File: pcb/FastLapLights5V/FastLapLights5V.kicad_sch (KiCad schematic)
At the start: 25 parts, among them IC1 74HCT1G125GV,125, J1 POWER_CON, J2 SWD, J3 I2C, J4 IO, U1 STM32C011F4Px, U2 AP63205WU, U3 AP2112K-3.3

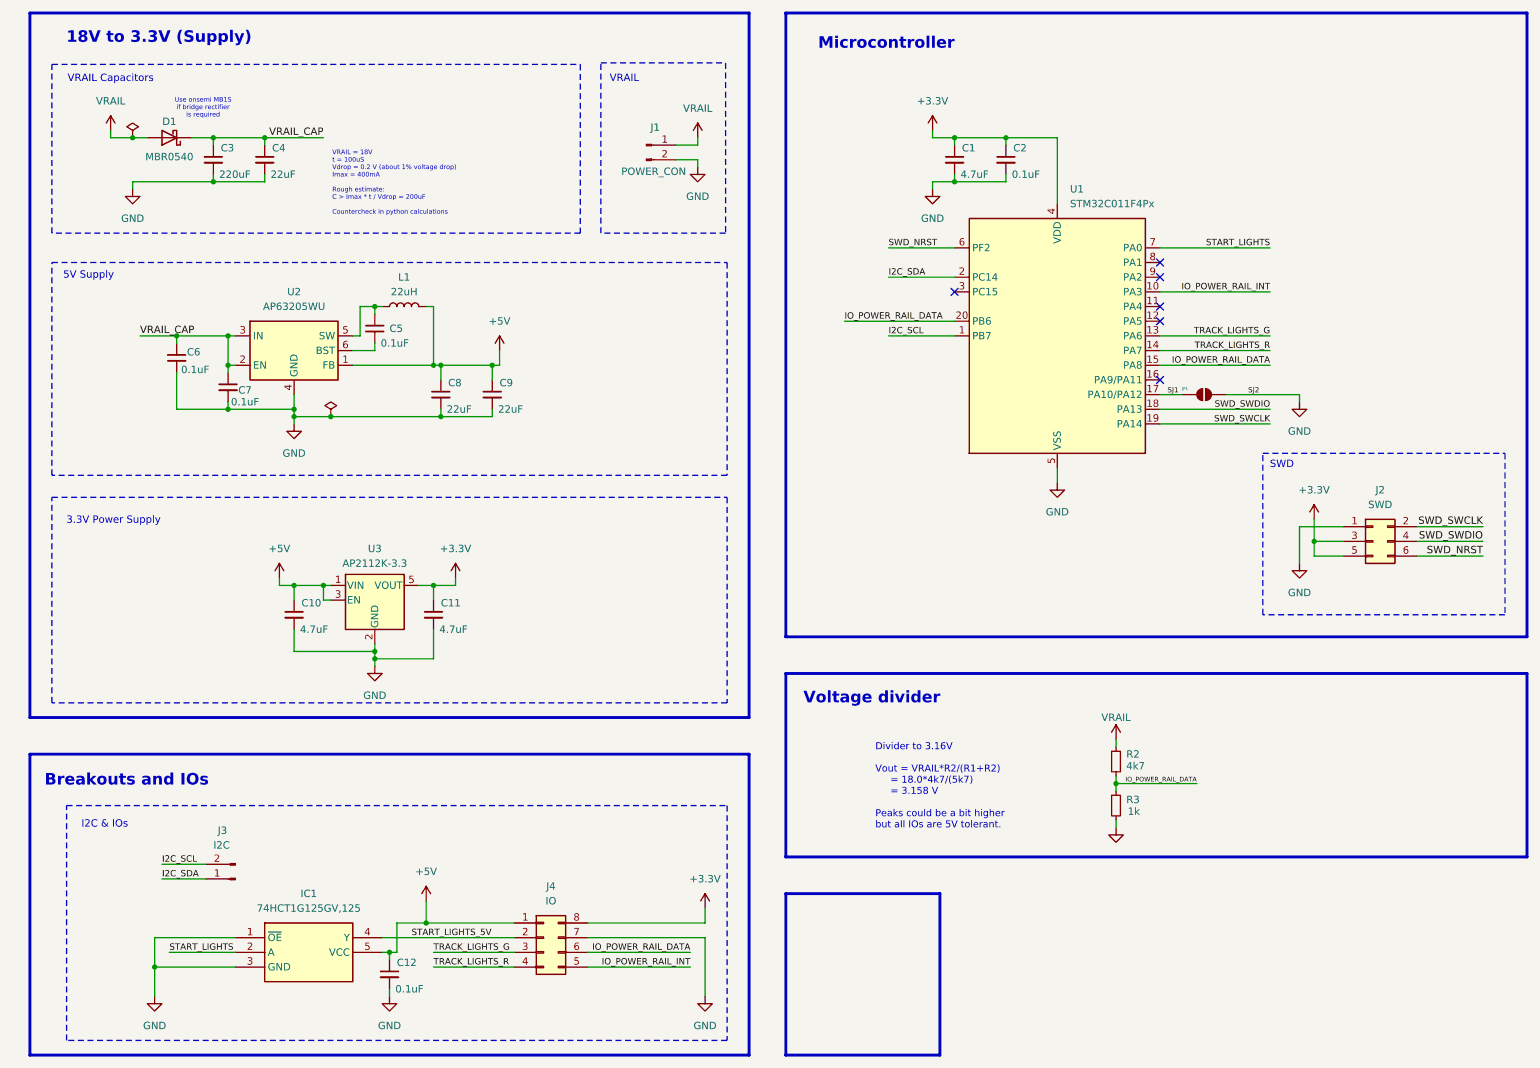
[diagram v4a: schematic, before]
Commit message: - add race mode practice session - i2c to uart for faster datastreaming to displays - fix timer issue with tim1
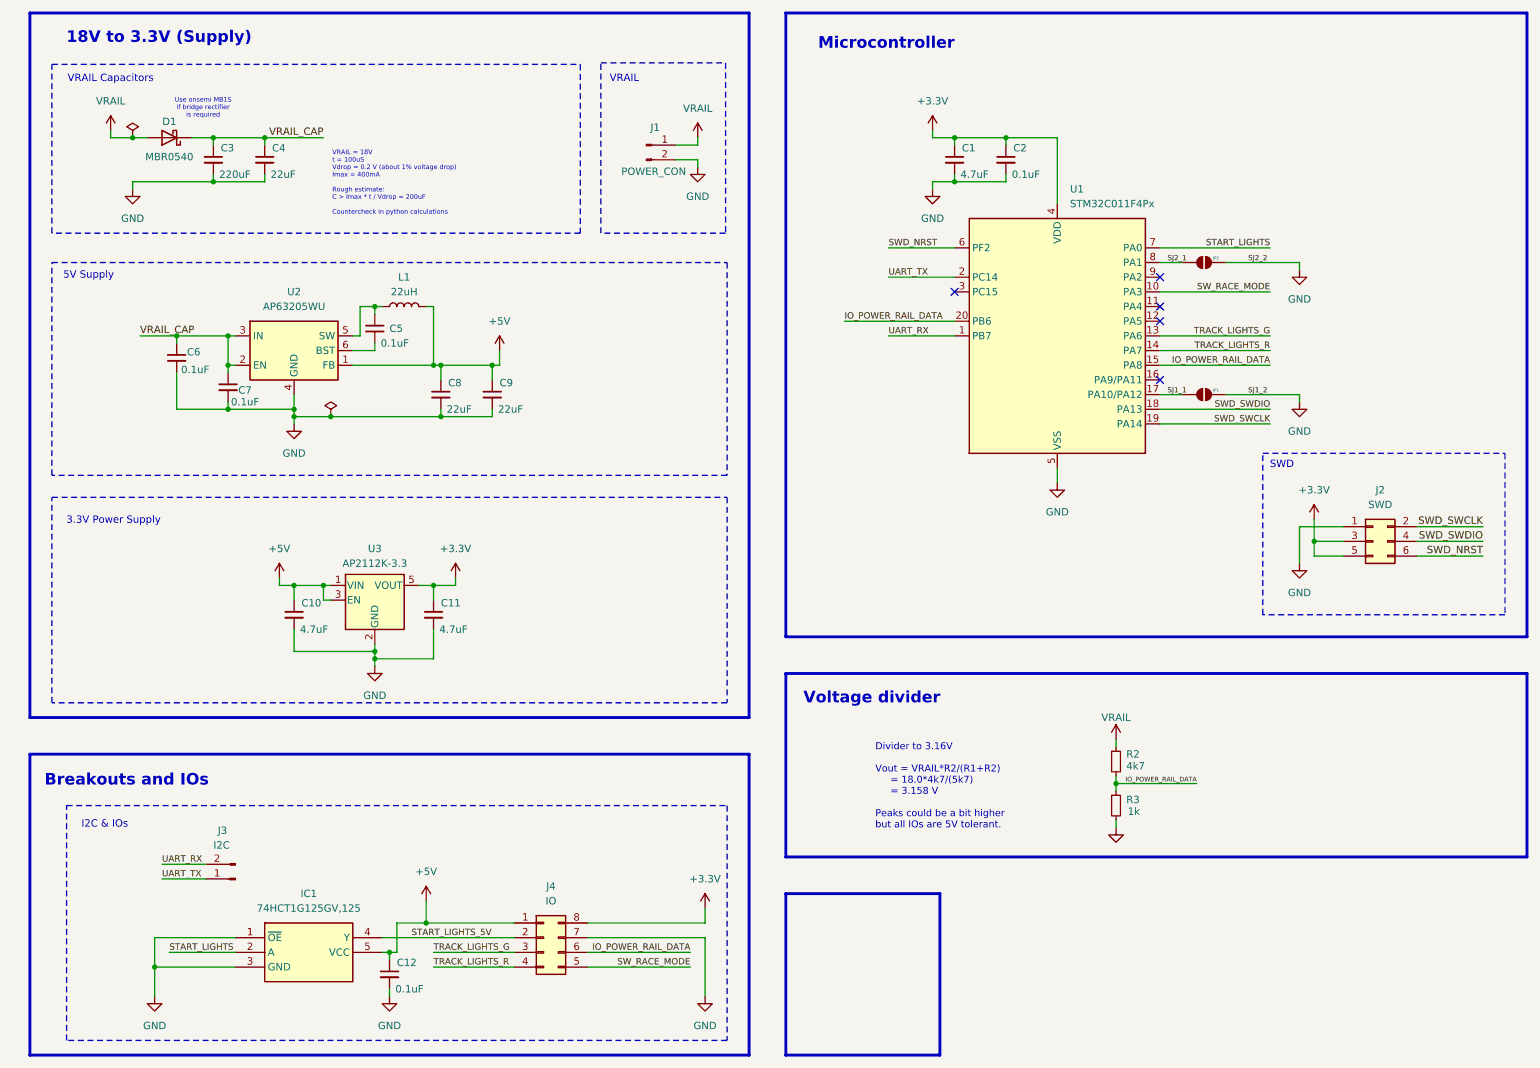
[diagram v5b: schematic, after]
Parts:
- added JP2: SP, Jumper:SolderJumper-2_P1.3mm_Open_RoundedPad1.0x1.5mm, symbol Jumper:SolderJumper_2_Open
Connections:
- net GND: now also JP2.2 (B)
- net SJ2_1: now reaches U1.8 (PA1)
- net SJ2_1: now also JP2.1 (A)
- net I2C_SCL renamed UART_RX
- net I2C_SDA renamed UART_TX
- net IO_POWER_RAIL_INT renamed SW_RACE_MODE
- net SJ1 renamed SJ1_1
- no-connect marks 6 -> 5
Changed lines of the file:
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@@
 	(title_block
 		(title "FastLapLights5V")
-		(date "2025-04-14")
-		(rev "MK6")
+		(date "2025-06-11")
+		(rev "MK7")
 		(comment 1 "18V Supply Power Rail")
 		(comment 2 "5V WS2812b PWR & SIG")
@@
 	)
 	(no_connect
-		(at 210.82 57.15)
-	)
-	(no_connect
 		(at 210.82 59.69)
 	)
@@
 	(wire
 		(pts
+			(xy 222.25 57.15) (xy 234.95 57.15)
+		)
+		(stroke
+			(width 0)
+			(type default)
+		)
+	)
+	(wire
+		(pts
 			(xy 210.82 62.23) (xy 229.87 62.23)
 		)
@@
 	(wire
 		(pts
+			(xy 210.82 57.15) (xy 214.63 57.15)
+		)
+		(stroke
+			(width 0)
+			(type default)
+		)
+	)
+	(wire
+		(pts
 			(xy 66.04 115.57) (xy 67.31 115.57)
 		)
@@
 	(wire
 		(pts
+			(xy 234.95 58.42) (xy 234.95 57.15)
+		)
+		(stroke
+			(width 0)
+			(type default)
+		)
+	)
+	(wire
+		(pts
 			(xy 78.74 176.53) (xy 78.74 171.45)
 		)
@@
 		)
 	)
+	(label "SJ2_2"
+		(at 226.06 57.15 0)
+		(effects
+			(font
+				(size 0.9 0.9)
+			)
+			(justify left bottom)
+		)
+	)
 	(label "SWD_SWDIO"
 		(at 229.87 82.55 180)
@@
 		)
 	)
-	(label "IO_POWER_RAIL_INT"
+	(label "SW_RACE_MODE"
 		(at 229.87 62.23 180)
 		(effects
@@
 		)
 	)
-	(label "SJ2"
+	(label "SJ1_2"
 		(at 226.06 80.01 0)
 		(effects
@@
 		)
 	)
-	(label "I2C_SDA"
+	(label "UART_TX"
 		(at 38.1 163.83 0)
 		(effects
@@
 		)
 	)
-	(label "I2C_SCL"
+	(label "UART_RX"
 		(at 38.1 161.29 0)
 		(effects
@@
 		)
 	)
-	(label "IO_POWER_RAIL_INT"
+	(label "SW_RACE_MODE"
 		(at 129.54 179.07 180)
 		(effects
@@
 		)
 	)
-	(label "I2C_SCL"
+	(label "UART_RX"
 		(at 163.83 69.85 0)
 		(effects
@@
 		)
 	)
+	(label "SJ2_1"
+		(at 212.09 57.15 0)
+		(effects
+			(font
+				(size 0.9 0.9)
+			)
+			(justify left bottom)
+		)
+	)
 	(label "SWD_SWDIO"
 		(at 266.7 105.41 180)
@@
 		)
 	)
-	(label "I2C_SDA"
+	(label "UART_TX"
 		(at 163.83 59.69 0)
 		(effects
@@
 		)
 	)
-	(label "SJ1"
+	(label "SJ1_1"
 		(at 212.09 80.01 0)
 		(effects
@@
 	)
 	(symbol
+		(lib_id "power:GND")
+		(at 234.95 58.42 0)
+		(unit 1)
+		(exclude_from_sim no)
+		(in_bom yes)
+		(on_board yes)
+		(dnp no)
+		(fields_autoplaced yes)
+		(property "Reference" "#PWR23"
+			(at 234.95 64.77 0)
+			(effects
+				(font
+					(size 1.27 1.27)
+				)
+				(hide yes)
+			)
+		)
+		(property "Value" "GND"
+			(at 234.95 63.5 0)
+			(effects
+				(font
+					(size 1.27 1.27)
+				)
+			)
+		)
+		(property "Footprint" ""
+			(at 234.95 58.42 0)
+			(effects
+				(font
+					(size 1.27 1.27)
+				)
+				(hide yes)
+			)
+		)
+		(property "Datasheet" ""
+			(at 234.95 58.42 0)
+			(effects
+				(font
+					(size 1.27 1.27)
+				)
+				(hide yes)
+			)
+		)
+		(property "Description" "Power symbol creates a global label with name \"GND\" , ground"
+			(at 234.95 58.42 0)
+			(effects
+				(font
+					(size 1.27 1.27)
+				)
+				(hide yes)
+			)
+		)
+		(pin "1"
+		)
+		(instances
+			(project "FastLapLights5V"
+				(path "/b6918c10-7d8e-4015-89e0-e42eef76cd26"
+					(reference "#PWR23")
+					(unit 1)
+				)
+			)
+		)
+	)
+	(symbol
 		(lib_id "Device:R_Small")
 		(at 203.2 143.51 0)
@@
 	)
 	(symbol
+		(lib_id "Jumper:SolderJumper_2_Open")
+		(at 218.44 57.15 0)
+		(unit 1)
+		(exclude_from_sim yes)
+		(in_bom no)
+		(on_board yes)
+		(dnp no)
+		(property "Reference" "JP2"
+			(at 220.472 56.388 0)
+			(effects
+				(font
+					(size 0.5 0.5)
+				)
+			)
+		)
+		(property "Value" "SP"
+			(at 218.44 53.34 0)
+			(effects
+				(font
+					(size 1.27 1.27)
+				)
+				(hide yes)
+			)
+		)
+		(property "Footprint" "Jumper:SolderJumper-2_P1.3mm_Open_RoundedPad1.0x1.5mm"
+			(at 218.44 57.15 0)
+			(effects
+				(font
+					(size 1.27 1.27)
+				)
+				(hide yes)
+			)
+		)
+		(property "Datasheet" "~"
+			(at 218.44 57.15 0)
+			(effects
+				(font
+					(size 1.27 1.27)
+				)
+				(hide yes)
+			)
+		)
+		(property "Description" "Solder Jumper, 2-pole, open"
+			(at 218.44 57.15 0)
+			(effects
+				(font
+					(size 1.27 1.27)
+				)
+				(hide yes)
+			)
+		)
+		(pin "2"
+		)
+		(pin "1"
+		)
+		(instances
+			(project "FastLapLights5V"
+				(path "/b6918c10-7d8e-4015-89e0-e42eef76cd26"
+					(reference "JP2")
+					(unit 1)
+				)
+			)
+		)
+	)
+	(symbol
 		(lib_id "power:+15V")
 		(at 29.21 34.29 0)
@@
 		(dnp no)
 		(property "Reference" "JP1"
-			(at 215.138 78.994 0)
+			(at 220.472 79.248 0)
 			(effects
 				(font

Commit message: fix workaround
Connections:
- net IO_POWER_RAIL_DATA: no longer U1.20 (PB6)
- no-connect marks 5 -> 6
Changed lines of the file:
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@@
 	(title_block
 		(title "FastLapLights5V")
-		(date "2025-06-11")
-		(rev "MK7")
+		(date "2025-10-14")
+		(rev "MK8")
 		(comment 1 "18V Supply Power Rail")
 		(comment 2 "5V WS2812b PWR & SIG")
@@
 	)
 	(no_connect
+		(at 175.26 67.31)
+	)
+	(no_connect
 		(at 210.82 59.69)
 	)
@@
 		(pts
 			(xy 255.27 102.87) (xy 266.7 102.87)
-		)
-		(stroke
-			(width 0)
-			(type default)
-		)
-	)
-	(wire
-		(pts
-			(xy 156.21 67.31) (xy 175.26 67.31)
 		)
 		(stroke
@@
 		(effects
 			(font
-				(size 1.1 1.1)
-			)
-			(justify left bottom)
-		)
-	)
-	(label "IO_POWER_RAIL_DATA"
-		(at 156.21 67.31 0)
-		(effects
-			(font
